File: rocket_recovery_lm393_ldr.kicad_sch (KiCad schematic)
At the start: 19 parts, among them J1 BAT 9V, J2 TRIGGER, J3 READY, J4 ON, Q1 BC548, Q2 TIP120, U1 LM7805, U2 LM393

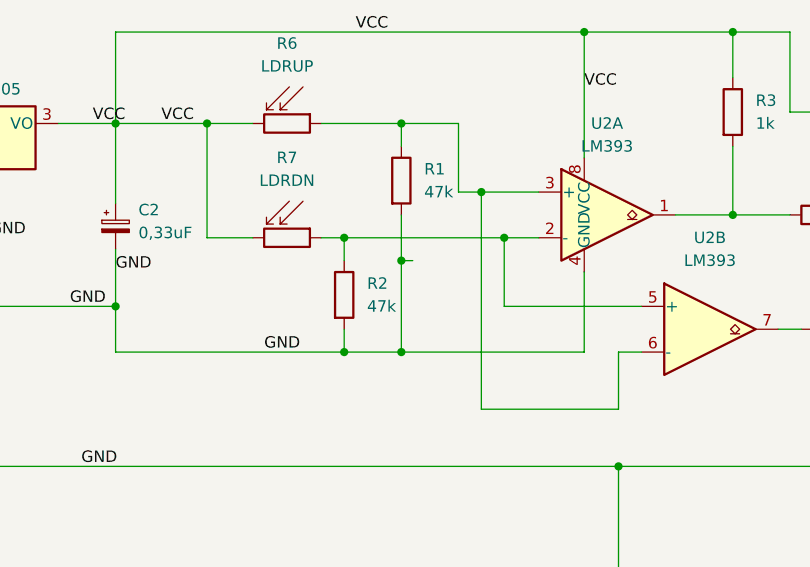
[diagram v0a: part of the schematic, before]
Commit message: Inversão sentido botão READY e ajustes de labels
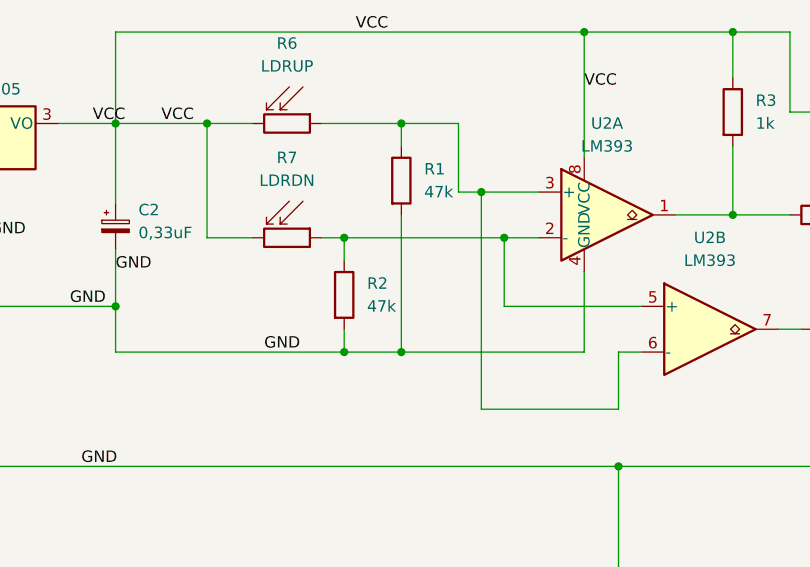
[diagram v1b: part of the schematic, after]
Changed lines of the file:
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@@
-	)
-	(junction
-		(at 105.41 53.34)
-		(diameter 0)
-		(color 0 0 0 0)
 	)
 	(junction
@@
 	(wire
 		(pts
-			(xy 105.41 53.34) (xy 106.68 53.34)
-		)
-		(stroke
-			(width 0)
-			(type default)
-		)
-	)
-	(wire
-		(pts
-			(xy 105.41 48.26) (xy 105.41 53.34)
+			(xy 105.41 48.26) (xy 105.41 63.5)
 		)
 		(stroke
@@
 		)
 		(stroke
-			(width 0)
-			(type default)
-		)
-	)
-	(wire
-		(pts
-			(xy 105.41 53.34) (xy 105.41 63.5)
-		)
-		(stroke
